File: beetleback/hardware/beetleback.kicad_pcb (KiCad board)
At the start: 4 copper layers, 20.8 x 28.3 mm, 25 parts, among them J1 Conn_01x05_Female, J3 motor_pad_1, J4 motor_pad_2, Q1 IRF7351TRPBF, Q2 IRF7351TRPBF, U1 ATtiny13A-SS, U2 DRV8701P

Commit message: reorganisation
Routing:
- net /GL1: track 17.0 -> 16.4 mm
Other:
- board text added: "GND"
- board text removed: "RX GND"
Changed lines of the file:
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@@
     (effects (font (size 1 1) (thickness 0.15)) (justify mirror))
   )
-  (gr_text "RX GND" (at 152 116.4 90) (layer "B.SilkS")
+  (gr_text "GND" (at 152 116.4 90) (layer "B.SilkS")
     (effects (font (size 1 1) (thickness 0.15)) (justify left mirror))
   )
@@
   (via (at 144.9 118.6) (size 0.8) (drill 0.4) (layers "F.Cu" "B.Cu") (net 1))
   (via (at 141.06498 120.2) (size 0.8) (drill 0.4) (layers "F.Cu" "B.Cu") (net 1))
-  (segment (start 144.9 118.6) (end 143.3 120.2) (width 0.2) (layer "B.Cu") (net 1))
-  (segment (start 143.3 120.2) (end 141.06498 120.2) (width 0.2) (layer "B.Cu") (net 1))
+  (segment (start 144.9 118.6) (end 141.06498 120.2) (width 0.2) (layer "B.Cu") (net 1))
   (segment (start 143.635 125.9) (end 143.635 126.875) (width 0.2) (layer "F.Cu") (net 2))
   (segment (start 141.76499 119.76499) (end 141.76499 124.02999) (width 0.2) (layer "F.Cu") (net 2))
@@
   (via (at 147.8 125.7) (size 0.8) (drill 0.4) (layers "F.Cu" "B.Cu") (net 4))
   (via (at 143.9 128.8) (size 0.8) (drill 0.4) (layers "F.Cu" "B.Cu") (net 4))
-  (segment (start 147.8 125.7) (end 145.3 125.7) (width 0.2) (layer "B.Cu") (net 4))
-  (segment (start 143.9 127.1) (end 143.9 128.8) (width 0.2) (layer "B.Cu") (net 4))
-  (segment (start 145.3 125.7) (end 143.9 127.1) (width 0.2) (layer "B.Cu") (net 4))
+  (segment (start 143.9 128.1) (end 143.9 128.8) (width 0.2) (layer "B.Cu") (net 4))
+  (segment (start 147.8 125.7) (end 146.3 125.7) (width 0.2) (layer "B.Cu") (net 4))
+  (segment (start 146.3 125.7) (end 143.9 128.1) (width 0.2) (layer "B.Cu") (net 4))
   (segment (start 151.413218 124.883099) (end 152.42158 124.883099) (width 0.2) (layer "F.Cu") (net 5))
   (segment (start 158.4 132.198026) (end 157.299102 133.298924) (width 0.2) (layer "F.Cu") (net 5))
@@
   (segment (start 141.9 116.7) (end 142 116.6) (width 0.2) (layer "F.Cu") (net 6))
   (via (at 142 116.6) (size 0.8) (drill 0.4) (layers "F.Cu" "B.Cu") (net 6))
+  (segment (start 142 116.6) (end 142 116) (width 0.2) (layer "B.Cu") (net 6))
   (segment (start 142.9 115.1) (end 147 115.1) (width 0.2) (layer "B.Cu") (net 6))
-  (segment (start 142.2 115.8) (end 142.9 115.1) (width 0.2) (layer "B.Cu") (net 6))
-  (segment (start 142 116.6) (end 142.2 116.4) (width 0.2) (layer "B.Cu") (net 6))
-  (segment (start 142.2 116.4) (end 142.2 115.8) (width 0.2) (layer "B.Cu") (net 6))
+  (segment (start 142 116) (end 142.9 115.1) (width 0.2) (layer "B.Cu") (net 6))
   (segment (start 159.346803 121.846803) (end 159.346803 122.8) (width 0.8) (layer "F.Cu") (net 7))
   (segment (start 145.201974 135.4) (end 145.201974 135.298026) (width 0.8) (layer "F.Cu") (net 7))
@@
   (segment (start 155.503051 129.403051) (end 155.503051 131.502872) (width 0.2) (layer "F.Cu") (net 8))
   (segment (start 150.413218 124.883099) (end 150.413218 125.348967) (width 0.2) (layer "F.Cu") (net 8))
-  (segment (start 153.801097 119.662899) (end 152.150718 121.313278) (width 0.2) (layer "F.Cu") (net 9))
+  (segment (start 152.150718 121.349282) (end 152.150718 121.645599) (width 0.2) (layer "F.Cu") (net 9))
   (segment (start 151.413218 120.908099) (end 152.150718 121.645599) (width 0.2) (layer "F.Cu") (net 9))
-  (segment (start 154.751 119.662899) (end 153.801097 119.662899) (width 0.2) (layer "F.Cu") (net 9))
-  (segment (start 152.150718 121.313278) (end 152.150718 121.645599) (width 0.2) (layer "F.Cu") (net 9))
+  (segment (start 153.837101 119.662899) (end 152.150718 121.349282) (width 0.2) (layer "F.Cu") (net 9))
+  (segment (start 154.751 119.662899) (end 153.837101 119.662899) (width 0.2) (layer "F.Cu") (net 9))
   (segment (start 156.382273 122.78547) (end 156.396803 122.8) (width 0.8) (layer "F.Cu") (net 10))
   (segment (start 156.396803 122.8) (end 157.7 122.8) (width 0.8) (layer "F.Cu") (net 10))

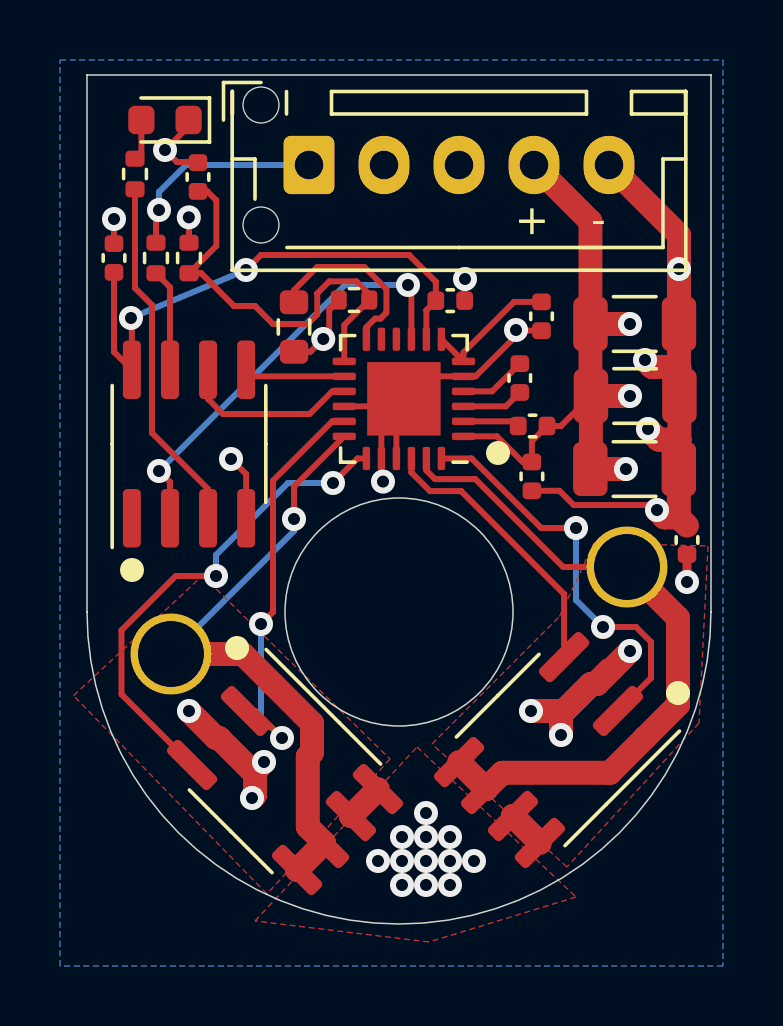
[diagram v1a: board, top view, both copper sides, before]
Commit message: Optional 5v regulator for RX
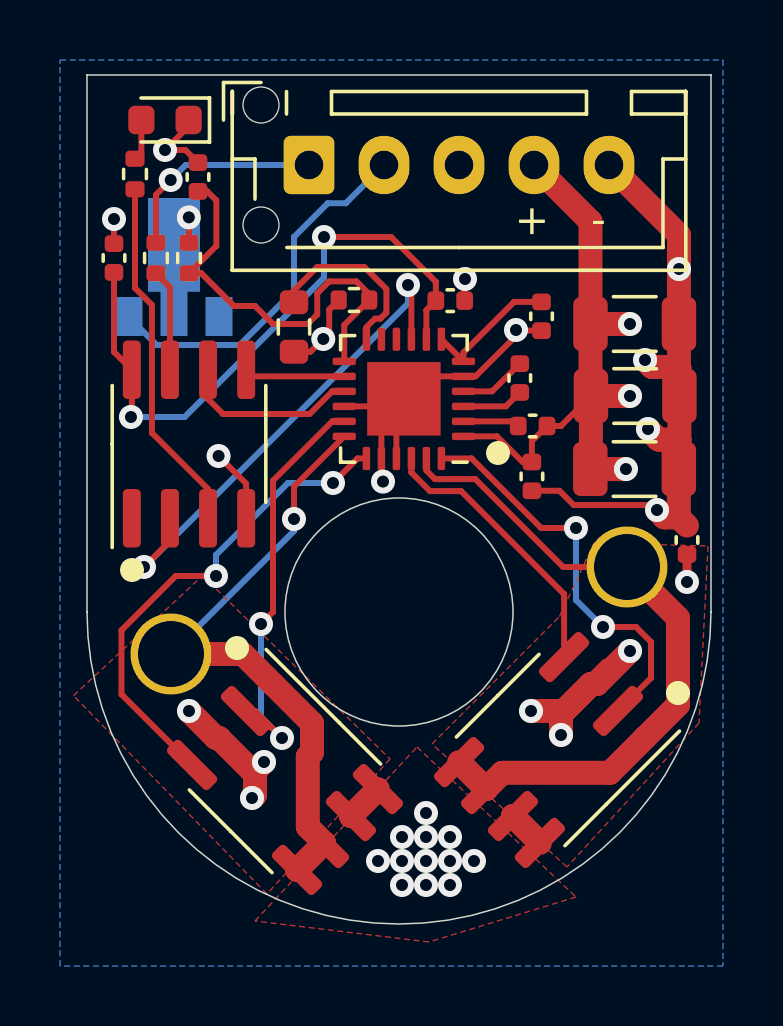
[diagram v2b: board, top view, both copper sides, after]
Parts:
- added U3: HT75xx-1-SOT89, Package_TO_SOT_SMD:SOT-89-3, B.Cu at (142.5, 118.5)
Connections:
- J1 pad 2: no_connect_23 -> +5V
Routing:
- net +5V: track 0.00 -> 12.4 mm
- net +3V3: track 18.3 -> 21.2 mm
- net /~FAULT: track 14.4 -> 16.9 mm

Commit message: slight tweak of 5v regulator
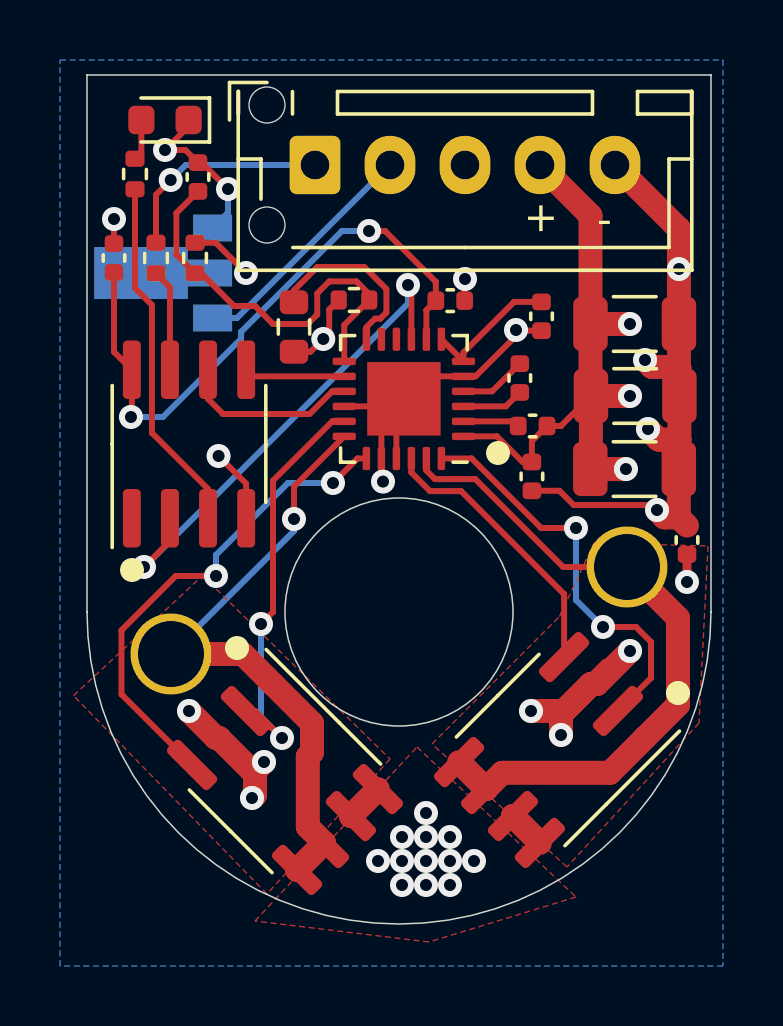
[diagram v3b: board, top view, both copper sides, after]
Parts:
- moved U3 0.41 mm to (142.1, 118.7), turned to 180 degrees
- moved J1 0.20 mm to (147.2, 115.1)
- moved R5 0.20 mm to (143.2, 118.2)
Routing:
- net +5V: track 12.4 -> 8.02 mm
- net GND: track 53.3 -> 56.3 mm, vias 17 -> 18
- net /VBAT: track 25.0 -> 26.2 mm
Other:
- board text added: "+5V"
- board text added: "BATT."

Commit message: Rev2 hardware: update mosfet, silkscreen tweaks, lcsc part numbers
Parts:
- Q1, Q2: value IRF7351TRPBF -> IRF8313PBF
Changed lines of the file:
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@@
     (descr "SOIC, 8 Pin (JEDEC MS-012AA, https://www.analog.com/media/en/package-pcb-resources/package/pkg_pdf/soic_narrow-r/r_8.pdf), generated with kicad-footprint-generator ipc_gullwing_generator.py")
     (tags "SOIC SO")
-    (property "LCSC" "C68403")
+    (property "LCSC" "C57696")
     (property "Sheet file" "beetleback.kicad_sch")
     (property "Sheet name" "")
@@
       (effects (font (size 1 1) (thickness 0.15)))
     )
-    (fp_text value "IRF7351TRPBF" (at 0 3.4 45) (layer "F.Fab") hide
+    (fp_text value "IRF8313PBF" (at 0 3.4 45) (layer "F.Fab") hide
       (effects (font (size 1 1) (thickness 0.15)))
     )
@@
     (descr "Resistor SMD 0402 (1005 Metric), square (rectangular) end terminal, IPC_7351 nominal, (Body size source: IPC-SM-782 page 72, https://www.pcb-3d.com/wordpress/wp-content/uploads/ipc-sm-782a_amendment_1_and_2.pdf), generated with kicad-footprint-generator")
     (tags "resistor")
-    (property "LCSC" "")
+    (property "LCSC" "C25879")
     (property "Sheet file" "beetleback.kicad_sch")
     (property "Sheet name" "")
@@
     (descr "SOIC, 8 Pin (JEDEC MS-012AA, https://www.analog.com/media/en/package-pcb-resources/package/pkg_pdf/soic_narrow-r/r_8.pdf), generated with kicad-footprint-generator ipc_gullwing_generator.py")
     (tags "SOIC SO")
-    (property "LCSC" "C68403")
+    (property "LCSC" "C57696")
     (property "Sheet file" "beetleback.kicad_sch")
     (property "Sheet name" "")
@@
       (effects (font (size 1 1) (thickness 0.15)))
     )
-    (fp_text value "IRF7351TRPBF" (at 0 3.4 135) (layer "F.Fab") hide
+    (fp_text value "IRF8313PBF" (at 0 3.4 135) (layer "F.Fab") hide
       (effects (font (size 1 1) (thickness 0.15)))
     )
@@
       (xy -0.21301 3.816417)) (layer "B.SilkS") (width 0) (fill solid))
   )
+  (gr_line (start 152.2 116.3) (end 152.2 118.7) (layer "B.SilkS") (width 0.12))
+  (gr_line (start 147.2 116.3) (end 147.2 117.9) (layer "B.SilkS") (width 0.12))
+  (gr_line (start 149.7 116.3) (end 149.7 118.7) (layer "B.SilkS") (width 0.12))
   (gr_circle (center 144.6 131.2) (end 144.8 131.2) (layer "F.SilkS") (width 0.4) (fill none))
   (gr_circle (center 159.3 132.7) (end 159.5 132.7) (layer "F.SilkS") (width 0.4) (fill none))
@@
     (effects (font (size 1 1) (thickness 0.15)) (justify left mirror))
   )
-  (gr_text "-" (at 157.1 116.4 90) (layer "B.SilkS")
+  (gr_text "-" (at 157.1 117.2 90) (layer "B.SilkS")
     (effects (font (size 1 1) (thickness 0.15)) (justify left mirror))
   )
-  (gr_text "RX IN" (at 147.2 116.5 90) (layer "B.SilkS")
+  (gr_text "RX IN" (at 147.2 118.4 90) (layer "B.SilkS")
     (effects (font (size 1 1) (thickness 0.15)) (justify left mirror))
   )
@@
     (effects (font (size 1 1) (thickness 0.15)) (justify mirror))
   )
-  (gr_text "GND" (at 152.2 116.8 90) (layer "B.SilkS")
+  (gr_text "GND" (at 152.2 119.4 90) (layer "B.SilkS")
     (effects (font (size 1 1) (thickness 0.15)) (justify left mirror))
   )
-  (gr_text "+5V" (at 149.7 118.2 90) (layer "B.SilkS")
+  (gr_text "+5V" (at 149.7 120.8 90) (layer "B.SilkS")
     (effects (font (size 1 1) (thickness 0.15)) (justify mirror))
   )
-  (gr_text "BATT." (at 155.8 118.2) (layer "B.SilkS")
+  (gr_text "BATT." (at 159.2 115.1 270) (layer "B.SilkS")
     (effects (font (size 1 1) (thickness 0.15)) (justify mirror))
   )
-  (gr_text "+" (at 154.7 116.3 90) (layer "B.SilkS")
+  (gr_text "+" (at 154.7 117.2 90) (layer "B.SilkS")
     (effects (font (size 1 1) (thickness 0.15)) (justify left mirror))
   )
